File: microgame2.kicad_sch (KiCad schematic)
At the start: 17 parts, among them SW9 SW_SPST, U1 ESP32-PICO-D4

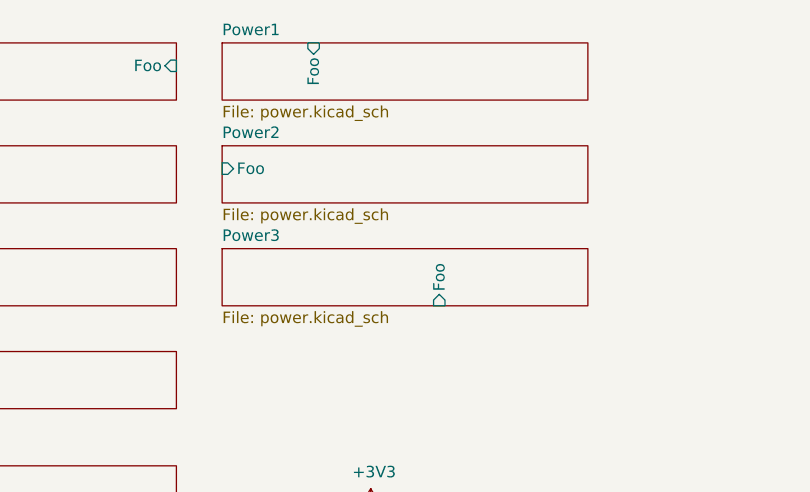
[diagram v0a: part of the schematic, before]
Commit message: reverting pin movement
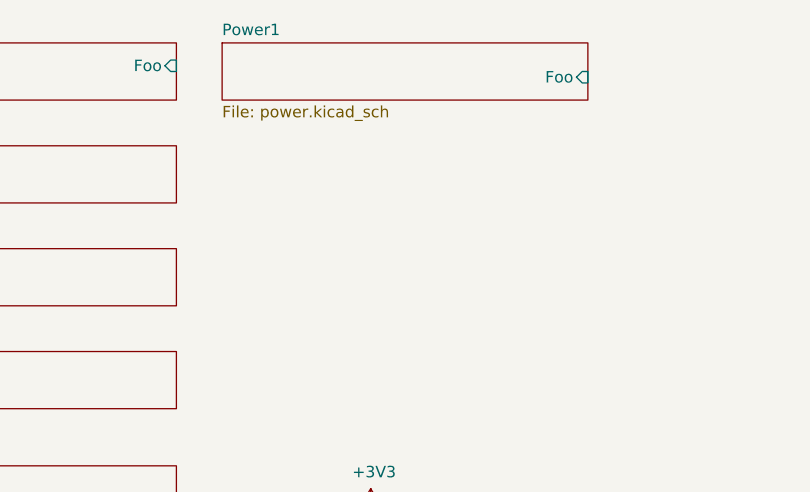
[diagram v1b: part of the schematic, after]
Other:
- removed sheet Power2
- removed sheet Power3
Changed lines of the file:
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@@
-	)
-	(sheet
-		(at 67.31 43.18)
-		(size 40.64 6.35)
-		(fields_autoplaced yes)
-		(stroke
-			(width 0)
-			(type solid)
-		)
-		(fill
-			(color 0 0 0 0.0000)
-		)
-		(property "Sheetname" "Power3"
-			(at 67.31 42.4684 0)
-			(effects
-				(font
-					(size 1.27 1.27)
-				)
-				(justify left bottom)
-			)
-		)
-		(property "Sheetfile" "power.kicad_sch"
-			(at 67.31 50.1146 0)
-			(effects
-				(font
-					(size 1.27 1.27)
-				)
-				(justify left top)
-			)
-		)
-		(pin "Foo" input
-			(at 91.44 49.53 270)
-			(effects
-				(font
-					(size 1.27 1.27)
-				)
-				(justify left)
-			)
-		)
-		(instances
-			(project "microgame2"
-				(path "/ebfd9da1-8e1c-4303-a1cc-72875a794180"
-					(page "9")
-				)
-			)
-		)
-	)
-	(sheet
-		(at 67.31 31.75)
-		(size 40.64 6.35)
-		(fields_autoplaced yes)
-		(stroke
-			(width 0)
-			(type solid)
-		)
-		(fill
-			(color 0 0 0 0.0000)
-		)
-		(property "Sheetname" "Power2"
-			(at 67.31 31.0384 0)
-			(effects
-				(font
-					(size 1.27 1.27)
-				)
-				(justify left bottom)
-			)
-		)
-		(property "Sheetfile" "power.kicad_sch"
-			(at 67.31 38.6846 0)
-			(effects
-				(font
-					(size 1.27 1.27)
-				)
-				(justify left top)
-			)
-		)
-		(pin "Foo" input
-			(at 67.31 34.29 180)
-			(effects
-				(font
-					(size 1.27 1.27)
-				)
-				(justify left)
-			)
-		)
-		(instances
-			(project "microgame2"
-				(path "/ebfd9da1-8e1c-4303-a1cc-72875a794180"
-					(page "8")
-				)
-			)
-		)
 	)
 	(sheet
@@
 		)
 		(pin "Foo" input
-			(at 77.47 20.32 90)
+			(at 107.95 24.13 0)
 			(effects
 				(font
